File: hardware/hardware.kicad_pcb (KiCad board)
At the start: 2 copper layers, 12.6 x 19.1 mm, 8 parts, among them IC1 ATTINY1634-MU, P1 CONN_01X05, P2 CONN_01X05

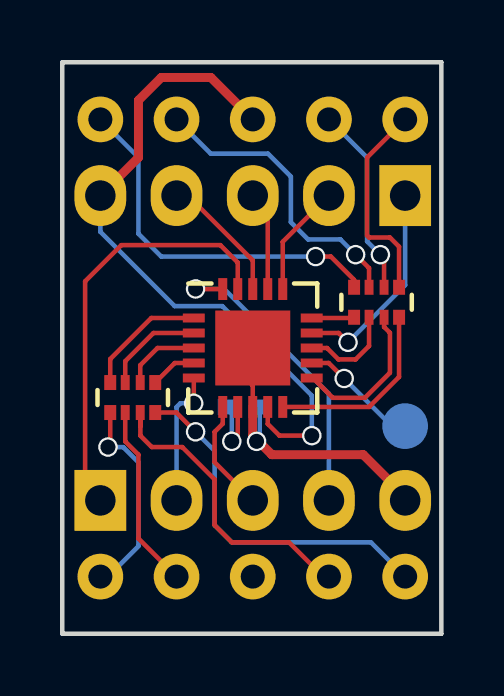
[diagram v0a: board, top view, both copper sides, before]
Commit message: + Add a 1uF decoupling capacitor to the power rails.
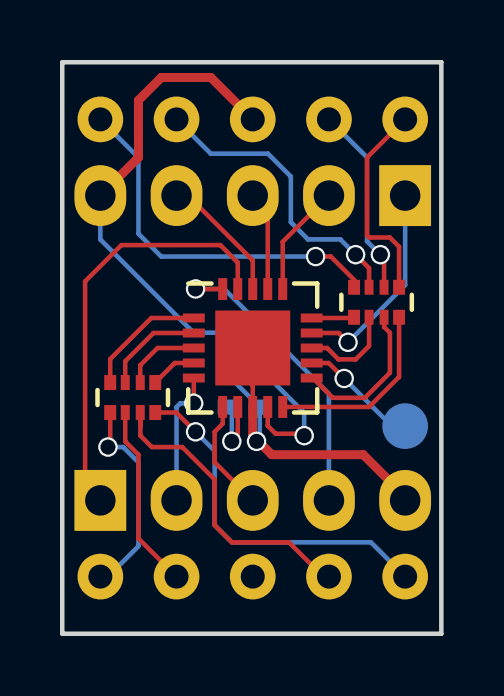
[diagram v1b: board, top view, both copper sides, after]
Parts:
- added C2: 1u, Capacitors_SMD:C_0402, B.Cu at (194.9, 109.9)
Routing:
- net GND: track 15.5 -> 17.2 mm
- net +5V: track 22.7 -> 22.0 mm
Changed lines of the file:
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@@
 (kicad_pcb (version 4) (host pcbnew 4.0.2+dfsg1-stable)
   (general
-    (links 34)
+    (links 36)
     (no_connects 0)
     (area 188.773999 99.619999 201.560501 118.820001)
     (thickness 1.6)
     (drawings 7)
-    (tracks 187)
+    (tracks 192)
     (zones 0)
-    (modules 8)
+    (modules 9)
     (nets 30)
   )
@@
     (visible_elements FFFFFF7F)
     (pcbplotparams
-      (layerselection 0x010f0_80000001)
+      (layerselection 0x01000_00000001)
       (usegerberextensions false)
       (excludeedgelayer true)
@@
       (padsonsilk false)
       (subtractmaskfromsilk false)
-      (outputformat 1)
+      (outputformat 4)
       (mirror false)
       (drillshape 0)
@@
     )
   )
+  (module Capacitors_SMD:C_0402 (layer B.Cu)
+    (at 194.8815 109.9185 180)
+    (descr "Capacitor SMD 0402, reflow soldering, AVX (see smccp.pdf)")
+    (tags "capacitor 0402")
+    (attr smd)
+    (fp_text reference C2 (at 0 1.7 180) (layer B.SilkS) hide
+      (effects (font (size 1 1) (thickness 0.15)) (justify mirror))
+    )
+    (fp_text value 1u (at 0 -1.7 180) (layer B.Fab) hide
+      (effects (font (size 1 1) (thickness 0.15)) (justify mirror))
+    )
+    (fp_line (start -1.15 0.6) (end 1.15 0.6) (layer B.CrtYd) (width 0.05))
+    (fp_line (start -1.15 -0.6) (end 1.15 -0.6) (layer B.CrtYd) (width 0.05))
+    (fp_line (start -1.15 0.6) (end -1.15 -0.6) (layer B.CrtYd) (width 0.05))
+    (fp_line (start 1.15 0.6) (end 1.15 -0.6) (layer B.CrtYd) (width 0.05))
+    (fp_line (start 0.25 0.475) (end -0.25 0.475) (layer B.SilkS) (width 0.15))
+    (fp_line (start -0.25 -0.475) (end 0.25 -0.475) (layer B.SilkS) (width 0.15))
+    (pad 1 smd rect (at -0.55 0 180) (size 0.6 0.5) (layers B.Cu B.Paste B.Mask)
+      (net 1 +5V))
+    (pad 2 smd rect (at 0.55 0 180) (size 0.6 0.5) (layers B.Cu B.Paste B.Mask)
+      (net 2 GND))
+    (model Capacitors_SMD.3dshapes/C_0402.wrl
+      (at (xyz 0 0 0))
+      (scale (xyz 1 1 1))
+      (rotate (xyz 0 0 0))
+    )
+  )
   (gr_text "GB\n'17" (at 189.1665 107.823) (layer B.SilkS)
     (effects (font (size 1.5 1.5) (thickness 0.3)) (justify right mirror))
@@
   (gr_line (start 188.849 118.745) (end 201.4855 118.745) (angle 90) (layer Edge.Cuts) (width 0.15))
   (gr_line (start 188.849 99.695) (end 188.849 118.745) (angle 90) (layer Edge.Cuts) (width 0.15))
-  (segment (start 195.699 111.185) (end 195.699 111.752) (width 0.1524) (layer F.Cu) (net 1))
-  (segment (start 190.119 105.3465) (end 190.119 104.14) (width 0.1524) (layer B.Cu) (net 1))
-  (segment (start 192.5955 107.823) (end 190.119 105.3465) (width 0.1524) (layer B.Cu) (net 1))
-  (segment (start 194.183 107.823) (end 192.5955 107.823) (width 0.1524) (layer B.Cu) (net 1))
-  (segment (start 197.1675 110.8075) (end 194.183 107.823) (width 0.1524) (layer B.Cu) (net 1))
-  (segment (start 197.1675 112.141) (end 197.1675 110.8075) (width 0.1524) (layer B.Cu) (net 1))
-  (via (at 197.1675 112.141) (size 0.65) (drill 0.5) (layers F.Cu B.Cu) (net 1))
-  (segment (start 196.088 112.141) (end 197.1675 112.141) (width 0.1524) (layer F.Cu) (net 1))
-  (segment (start 195.699 111.752) (end 196.088 112.141) (width 0.1524) (layer F.Cu) (net 1))
+  (segment (start 195.4315 109.9185) (end 195.453 109.9185) (width 0.1524) (layer B.Cu) (net 1) (status C00000))
+  (segment (start 195.453 109.9185) (end 196.9135 111.379) (width 0.1524) (layer B.Cu) (net 1) (status 400000))
+  (segment (start 195.699 111.8155) (end 195.699 111.185) (width 0.1524) (layer F.Cu) (net 1) (status 800000))
+  (segment (start 195.961 112.0775) (end 195.699 111.8155) (width 0.1524) (layer F.Cu) (net 1))
+  (segment (start 196.85 112.0775) (end 195.961 112.0775) (width 0.1524) (layer F.Cu) (net 1))
+  (segment (start 196.9135 112.141) (end 196.85 112.0775) (width 0.1524) (layer F.Cu) (net 1))
+  (via (at 196.9135 112.141) (size 0.65) (drill 0.5) (layers F.Cu B.Cu) (net 1))
+  (segment (start 196.9135 111.379) (end 196.9135 112.141) (width 0.1524) (layer B.Cu) (net 1))
+  (segment (start 190.119 104.14) (end 190.119 105.6005) (width 0.1524) (layer B.Cu) (net 1) (status 400000))
+  (segment (start 194.225 108.712) (end 195.4315 109.9185) (width 0.1524) (layer B.Cu) (net 1) (status 800000))
+  (segment (start 193.2305 108.712) (end 194.225 108.712) (width 0.1524) (layer B.Cu) (net 1))
+  (segment (start 190.119 105.6005) (end 193.2305 108.712) (width 0.1524) (layer B.Cu) (net 1))
   (segment (start 195.199 101.6) (end 193.802 100.203) (width 0.3) (layer F.Cu) (net 1))
   (segment (start 193.802 100.203) (end 192.151 100.203) (width 0.3) (layer F.Cu) (net 1))
@@
   (segment (start 191.389 102.87) (end 190.119 104.14) (width 0.3) (layer F.Cu) (net 1))
   (segment (start 190.119 104.14) (end 190.119 103.886) (width 0.1524) (layer F.Cu) (net 1))
+  (segment (start 194.3315 109.9185) (end 194.3315 110.0885) (width 0.1524) (layer B.Cu) (net 2) (status C00000))
+  (segment (start 194.3315 110.0885) (end 195.4315 111.1885) (width 0.1524) (layer B.Cu) (net 2) (status C00000))
   (segment (start 195.4315 111.1885) (end 195.4315 112.226) (width 0.1524) (layer B.Cu) (net 2))
   (via (at 195.326 112.3315) (size 0.65) (drill 0.5) (layers F.Cu B.Cu) (net 2))
